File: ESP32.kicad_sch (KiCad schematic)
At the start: 18 parts, among them J2 Conn_01x08, J3 Conn_01x04, J4 USB_C_Receptacle_USB2.0, J8 TC2030-IDC, SW1 SWITCH-SPST, SW2 SWITCH-SPST, U6 ESP32-S3-WROOM-1

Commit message: lots of routing
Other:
- title: bitaxeGamma Turbo -> bitaxeNaja
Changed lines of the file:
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@@
 	(paper "A4")
 	(title_block
-		(title "bitaxeGamma Turbo")
-		(date "2025-05-12")
-		(rev "800xxx")
+		(title "bitaxeNaja")
+		(date "2025-07-17")
+		(rev "1200x")
 	)
 	(text "OLED Display Header\nSSD1306 128x32 I2C OLED"

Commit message: placed and routed and DRC'd. updated TPS546 for 1.0V output.
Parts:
- TP29: value TestPoint -> EN
- TP32: value TestPoint -> TX
- TP33: value TestPoint -> RX
- TP34: value TestPoint -> 3V3
- TP35: value TestPoint -> GND
- TP36: value TestPoint -> IO0
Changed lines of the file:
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@@
 			)
 		)
-		(property "Value" "TestPoint"
+		(property "Value" "IO0"
 			(at 150.495 158.7501 90)
 			(effects
@@
 			)
 		)
-		(property "Value" "TestPoint"
+		(property "Value" "GND"
 			(at 150.495 156.2101 90)
 			(effects
@@
 			)
 		)
-		(property "Value" "TestPoint"
+		(property "Value" "EN"
 			(at 106.045 156.2099 90)
 			(effects
@@
 			)
 		)
-		(property "Value" "TestPoint"
+		(property "Value" "TX"
 			(at 106.045 158.7499 90)
 			(effects
@@
 			)
 		)
-		(property "Value" "TestPoint"
+		(property "Value" "3V3"
 			(at 150.495 153.6701 90)
 			(effects
@@
 			)
 		)
-		(property "Value" "TestPoint"
+		(property "Value" "RX"
 			(at 106.045 161.2899 90)
 			(effects

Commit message: update to KiCad 10
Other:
- company: (none) -> bitaxeorg

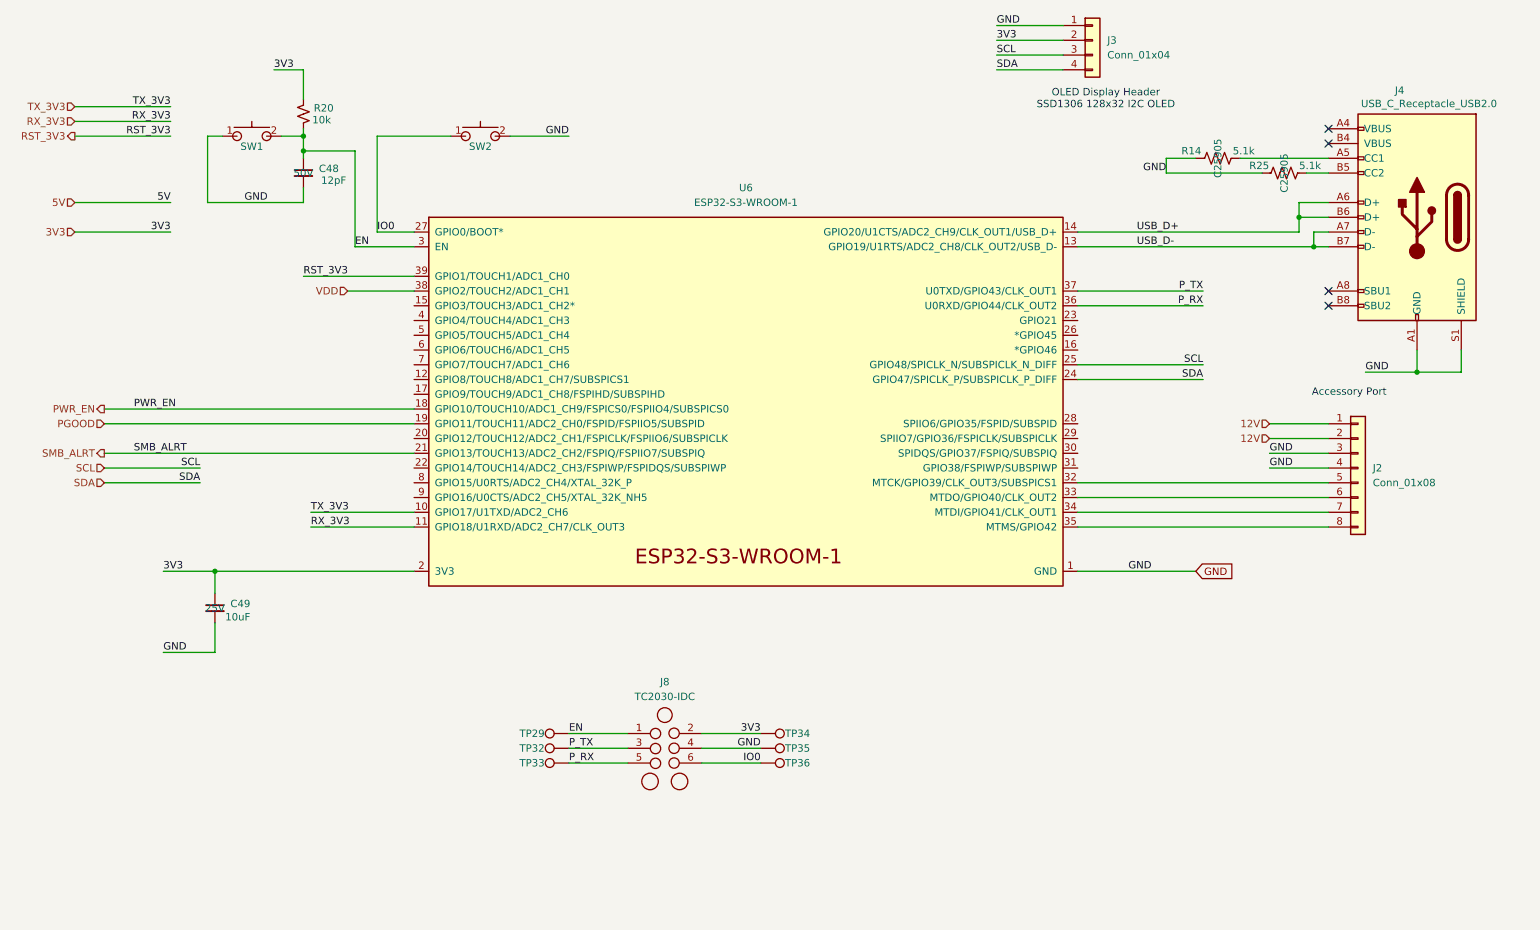
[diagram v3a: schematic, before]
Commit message: switched to single phase TPS546D24 and put the ASICs in series.
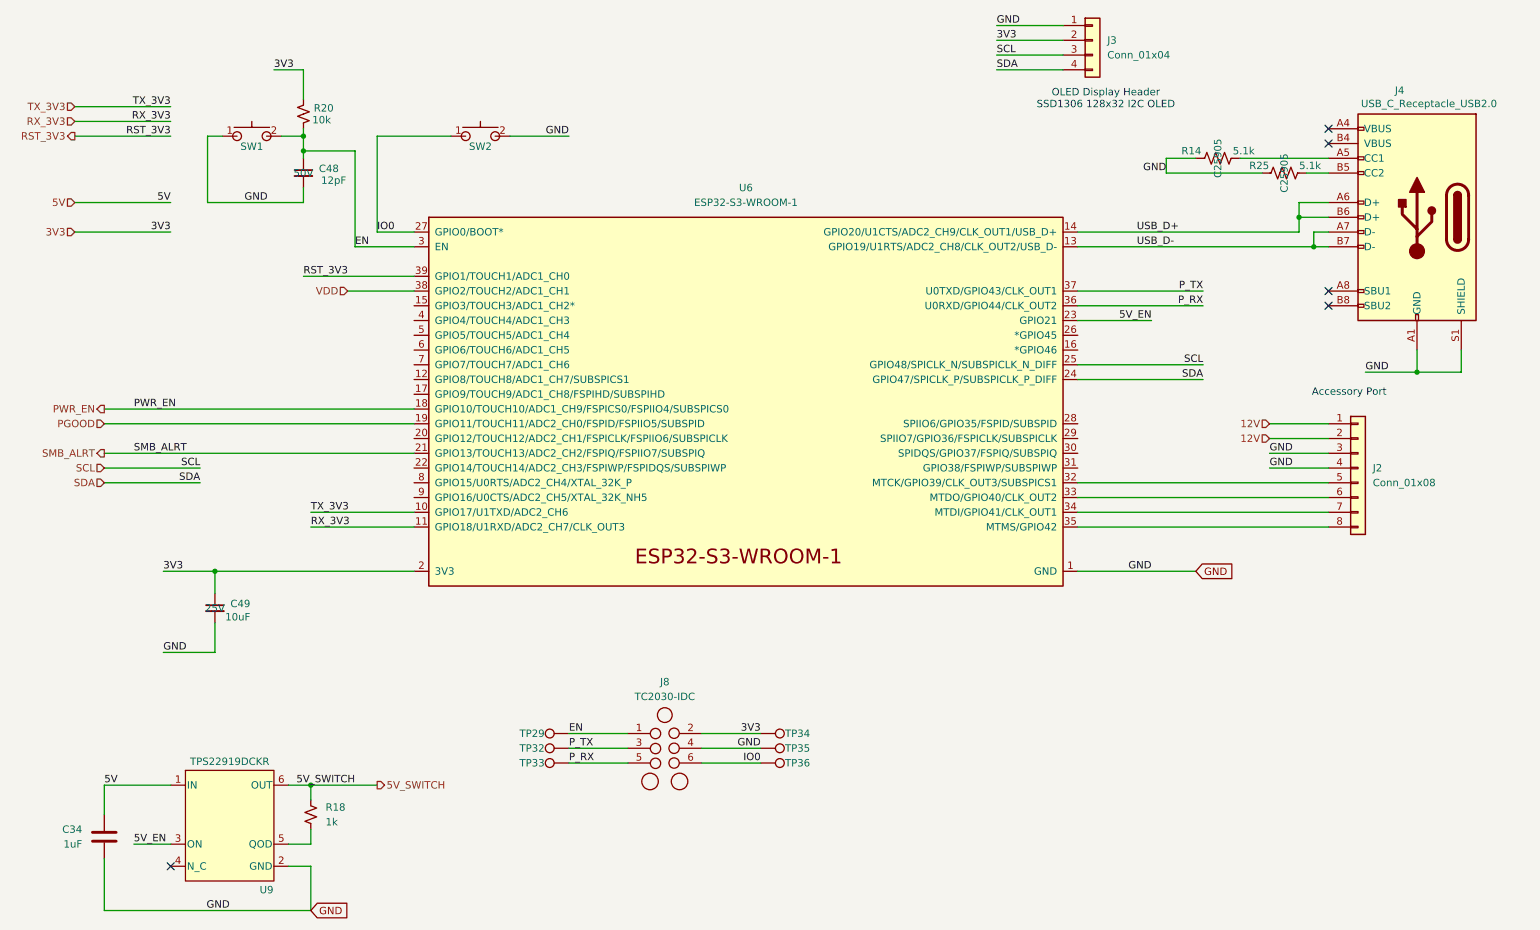
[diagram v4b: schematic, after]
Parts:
- added C34: 1uF, Capacitor_SMD:C_0402_1005Metric, symbol Device:C
- added R18: 1k, Resistor_SMD:R_0402_1005Metric, symbol Device:R_Small_US
- added U9: TPS22919DCKR, bitaxe:DCK0006A_N, symbol bitaxe:TPS22919DCKR
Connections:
- net 5V: now also C34.1, U9.1 (IN)
- net GND: now also C34.2, U9.2 (GND)
- net 5V_EN: now reaches U6.23 (GPIO21)
- net 5V_EN: now also U9.3 (ON)
- new net: R18.2, U9.5 (QOD)
- new net 5V_SWITCH: R18.1, U9.6 (OUT)
- no-connect marks 4 -> 5

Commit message: finished placing parts. lots of routing.
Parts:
- removed J8: TC2030-IDC, Connector:Tag-Connect_TC2030-IDC-NL_2x03_P1.27mm_Vertical, symbol bitaxe:TC2030-IDC-NL
- removed TP29: EN, TestPoint:TestPoint_Pad_D1.5mm, symbol Connector:TestPoint
- removed TP32: TX, TestPoint:TestPoint_Pad_D1.5mm, symbol Connector:TestPoint
- removed TP33: RX, TestPoint:TestPoint_Pad_D1.5mm, symbol Connector:TestPoint
- removed TP34: 3V3, TestPoint:TestPoint_Pad_D1.5mm, symbol Connector:TestPoint
- removed TP35: GND, TestPoint:TestPoint_Pad_D1.5mm, symbol Connector:TestPoint
- removed TP36: IO0, TestPoint:TestPoint_Pad_D1.5mm, symbol Connector:TestPoint
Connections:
- net P_RX: no longer names the net of U6.36 (U0RXD/GPIO44/CLK_OUT2)
- net P_TX: no longer names the net of U6.37 (U0TXD/GPIO43/CLK_OUT1)
- net VDD: no longer names the net of U6.38 (GPIO2/TOUCH2/ADC1_CH1)
- no-connect marks 5 -> 25

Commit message: AI BOM updates
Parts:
- C34: LCSC C52923 -> C2177690
- C49: LCSC (none) -> C344022
- R14, R25: LCSC C25905 -> C2481753
- R20: LCSC (none) -> C25744
- U6: value ESP32-S3-WROOM-1 -> ESP32-S3-WROOM-1-N16R8; DK 1965-ESP32-S3-WROOM-1-N16R8CT-ND -> 5407-ESP32-S3-WROOM-1-N16R8TR-ND
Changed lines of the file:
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@@
+			)
+		)
+		(property "Mouser" ""
+			(at 96.52 52.07 0)
+			(hide yes)
+			(show_name no)
+			(do_not_autoplace no)
+			(effects
+				(font
+					(size 1.27 1.27)
+				)
 			)
 		)
@@
 		)
 		(property "PARTNO" "FFC2B35-08-T"
+			(at 247.65 109.22 0)
+			(hide yes)
+			(show_name no)
+			(do_not_autoplace no)
+			(effects
+				(font
+					(size 1.27 1.27)
+				)
+			)
+		)
+		(property "Mouser" ""
 			(at 247.65 109.22 0)
 			(hide yes)
@@
 			)
 		)
+		(property "Mouser" ""
+			(at 67.31 168.91 0)
+			(hide yes)
+			(show_name no)
+			(do_not_autoplace no)
+			(effects
+				(font
+					(size 1.27 1.27)
+				)
+			)
+		)
 		(pin "1"
 		)
@@
 			)
 		)
-		(property "LCSC" "C52923"
+		(property "LCSC" "C2177690"
 			(at 31.75 172.72 0)
 			(hide yes)
@@
 		)
 		(property "Sim.Pins" ""
+			(at 31.75 172.72 0)
+			(hide yes)
+			(show_name no)
+			(do_not_autoplace no)
+			(effects
+				(font
+					(size 1.27 1.27)
+				)
+			)
+		)
+		(property "Mouser" ""
 			(at 31.75 172.72 0)
 			(hide yes)
@@
 			)
 		)
+		(property "Mouser" ""
+			(at 257.81 66.04 0)
+			(hide yes)
+			(show_name no)
+			(do_not_autoplace no)
+			(effects
+				(font
+					(size 1.27 1.27)
+				)
+			)
+		)
 		(pin "B7"
 		)
@@
 			)
 		)
-		(property "LCSC" "C25905"
+		(property "LCSC" "C2481753"
 			(at 234.95 58.42 0)
+			(show_name no)
+			(do_not_autoplace no)
+			(effects
+				(font
+					(size 1.27 1.27)
+				)
+			)
+		)
+		(property "Mouser" ""
+			(at 234.95 58.42 90)
+			(hide yes)
 			(show_name no)
 			(do_not_autoplace no)
@@
 		(property "Voltage" "25V"
 			(at 50.8 133.35 0)
+			(show_name no)
+			(do_not_autoplace no)
+			(effects
+				(font
+					(size 1.27 1.27)
+				)
+			)
+		)
+		(property "LCSC" "C344022"
+			(at 50.8 133.35 0)
+			(hide yes)
+			(show_name no)
+			(do_not_autoplace no)
+			(effects
+				(font
+					(size 1.27 1.27)
+				)
+			)
+		)
+		(property "Mouser" ""
+			(at 50.8 133.35 0)
+			(hide yes)
 			(show_name no)
 			(do_not_autoplace no)
@@
 			)
 		)
-		(property "Value" "ESP32-S3-WROOM-1"
+		(property "Value" "ESP32-S3-WROOM-1-N16R8"
 			(at 142.24 63.5 0)
 			(show_name no)
@@
 			)
 		)
-		(property "DK" "1965-ESP32-S3-WROOM-1-N16R8CT-ND"
+		(property "DK" "5407-ESP32-S3-WROOM-1-N16R8TR-ND"
 			(at 140.97 99.06 0)
 			(hide yes)
@@
 		)
 		(property "PARTNO" "ESP32-S3-WROOM-1-N16R8"
+			(at 140.97 99.06 0)
+			(hide yes)
+			(show_name no)
+			(do_not_autoplace no)
+			(effects
+				(font
+					(size 1.27 1.27)
+				)
+			)
+		)
+		(property "Mouser" ""
 			(at 140.97 99.06 0)
 			(hide yes)
@@
 			)
 		)
+		(property "Mouser" ""
+			(at 57.15 52.07 0)
+			(hide yes)
+			(show_name no)
+			(do_not_autoplace no)
+			(effects
+				(font
+					(size 1.27 1.27)
+				)
+			)
+		)
 		(pin "2"
 		)
@@
 			)
 		)
+		(property "Mouser" ""
+			(at 201.93 35.56 0)
+			(hide yes)
+			(show_name no)
+			(do_not_autoplace no)
+			(effects
+				(font
+					(size 1.27 1.27)
+				)
+			)
+		)
 		(pin "4"
 		)
@@
 			)
 		)
+		(property "LCSC" "C25744"
+			(at 66.04 48.26 0)
+			(hide yes)
+			(show_name no)
+			(do_not_autoplace no)
+			(effects
+				(font
+					(size 1.27 1.27)
+				)
+			)
+		)
+		(property "Mouser" ""
+			(at 66.04 48.26 0)
+			(hide yes)
+			(show_name no)
+			(do_not_autoplace no)
+			(effects
+				(font
+					(size 1.27 1.27)
+				)
+			)
+		)
 		(pin "2"
 		)
@@
 			)
 		)
+		(property "Mouser" ""
+			(at 66.04 58.42 0)
+			(hide yes)
+			(show_name no)
+			(do_not_autoplace no)
+			(effects
+				(font
+					(size 1.27 1.27)
+				)
+			)
+		)
 		(pin "1"
 		)
@@
 			)
 		)
+		(property "Mouser" ""
+			(at 53.34 171.45 0)
+			(hide yes)
+			(show_name no)
+			(do_not_autoplace no)
+			(effects
+				(font
+					(size 1.27 1.27)
+				)
+			)
+		)
 		(pin "1"
 		)
@@
 			)
 		)
-		(property "LCSC" "C25905"
+		(property "LCSC" "C2481753"
 			(at 223.52 55.88 0)
 			(show_name no)
 			(do_not_autoplace no)
+			(effects
+				(font
+					(size 1.27 1.27)
+				)
+			)
+		)
+		(property "Mouser" ""
+			(at 223.52 55.88 90)
+			(hide yes)
+			(show_name no)
+			(do_not_autoplace no)
